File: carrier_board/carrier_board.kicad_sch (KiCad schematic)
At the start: 4 parts, among them J1 47571-0001, U1 Pico

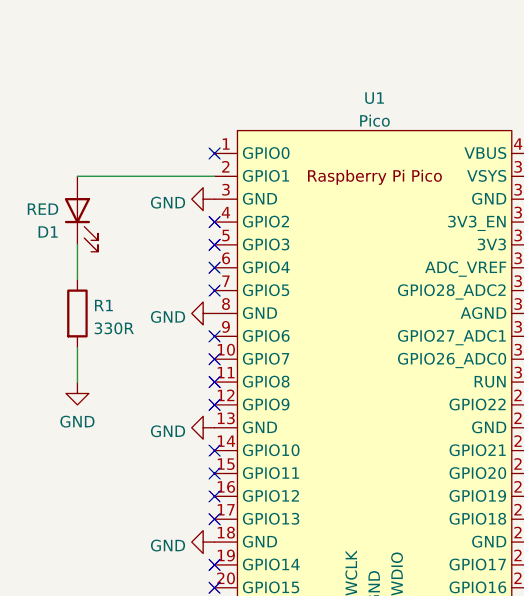
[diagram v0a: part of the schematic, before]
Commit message: Change red LED from GP2 to GP4 to free up UART RX
Also add label to LED on board
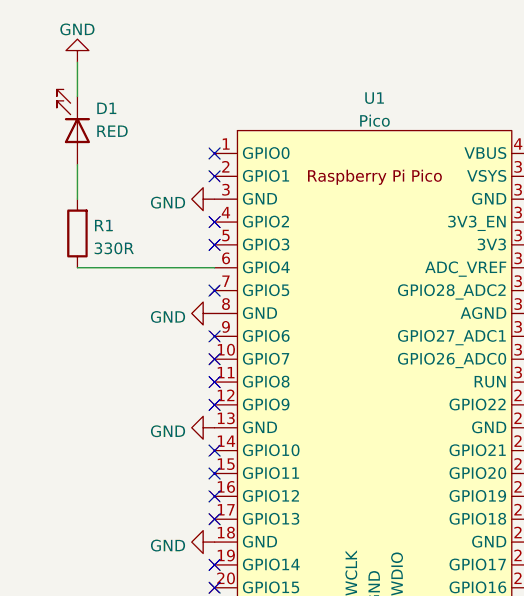
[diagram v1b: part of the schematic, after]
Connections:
- net GND: now also D1.1 (K); no longer R1.2
- net at R1.1: now also U1.6 (GPIO4); no longer D1.1 (K)
- net at D1.2 (A): now also R1.2; no longer U1.2 (GPIO1)
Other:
- moved on the sheet: D1, R1
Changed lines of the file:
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@@
     (title "OpenReset Carrier Board")
     (date "2022-03-20")
-    (rev "v1")
+    (rev "v1a")
     (company "cyanic")
   )
@@
   (no_connect (at 127 68.58))
   (no_connect (at 127 63.5))
-  (no_connect (at 127 60.96))
   (no_connect (at 127 58.42))
   (no_connect (at 127 55.88))
@@
   (no_connect (at 127 81.28))
   (no_connect (at 127 76.2))
+  (no_connect (at 127 50.8))
   (no_connect (at 127 96.52))
   (no_connect (at 142.24 101.6))
@@
     (stroke (width 0) (type default) (color 0 0 0 0))
   )
-  (wire (pts (xy 111.76 69.85) (xy 111.76 73.66))
-    (stroke (width 0) (type default) (color 0 0 0 0))
-  )
   (wire (pts (xy 124.46 129.54) (xy 124.46 134.62))
     (stroke (width 0) (type default) (color 0 0 0 0))
@@
     (stroke (width 0) (type default) (color 0 0 0 0))
   )
-  (wire (pts (xy 111.76 50.8) (xy 127 50.8))
+  (wire (pts (xy 111.76 38.1) (xy 111.76 41.91))
     (stroke (width 0) (type default) (color 0 0 0 0))
   )
@@
     (stroke (width 0) (type default) (color 0 0 0 0))
   )
-  (wire (pts (xy 111.76 58.42) (xy 111.76 62.23))
+  (wire (pts (xy 111.76 60.96) (xy 127 60.96))
+    (stroke (width 0) (type default) (color 0 0 0 0))
+  )
+  (wire (pts (xy 111.76 49.53) (xy 111.76 53.34))
     (stroke (width 0) (type default) (color 0 0 0 0))
   )
@@
     (pin "1")
   )
-  (symbol (lib_id "Device:LED") (at 111.76 54.61 90) (unit 1)
+  (symbol (lib_id "Device:LED") (at 111.76 45.72 270) (unit 1)
     (in_bom yes) (on_board yes)
-    (property "Reference" "D1" (id 0) (at 109.728 57.0322 90)
+    (property "Reference" "D1" (id 0) (at 113.792 43.2978 90)
       (effects (font (size 1.27 1.27)) (justify left))
     )
-    (property "Value" "RED" (id 1) (at 109.728 54.4953 90)
+    (property "Value" "RED" (id 1) (at 113.792 45.8347 90)
       (effects (font (size 1.27 1.27)) (justify left))
     )
-    (property "Footprint" "Library:LED_0603_1608Metric_Pad1.05x0.95mm_HandSolder" (id 2) (at 111.76 54.61 0)
-      (effects (font (size 1.27 1.27)) hide)
-    )
-    (property "Datasheet" "~" (id 3) (at 111.76 54.61 0)
+    (property "Footprint" "Library:LED_0603_1608Metric_Pad1.05x0.95mm_HandSolder" (id 2) (at 111.76 45.72 0)
+      (effects (font (size 1.27 1.27)) hide)
+    )
+    (property "Datasheet" "~" (id 3) (at 111.76 45.72 0)
       (effects (font (size 1.27 1.27)) hide)
     )
@@
     (pin "1")
   )
-  (symbol (lib_id "Device:R") (at 111.76 66.04 0) (unit 1)
-    (in_bom yes) (on_board yes) (fields_autoplaced)
-    (property "Reference" "R1" (id 0) (at 113.538 65.2053 0)
-      (effects (font (size 1.27 1.27)) (justify left))
-    )
-    (property "Value" "330R" (id 1) (at 113.538 67.7422 0)
-      (effects (font (size 1.27 1.27)) (justify left))
-    )
-    (property "Footprint" "Library:R_0603_1608Metric_Pad0.98x0.95mm_HandSolder" (id 2) (at 109.982 66.04 90)
-      (effects (font (size 1.27 1.27)) hide)
-    )
-    (property "Datasheet" "~" (id 3) (at 111.76 66.04 0)
+  (symbol (lib_id "Device:R") (at 111.76 57.15 180) (unit 1)
+    (in_bom yes) (on_board yes) (fields_autoplaced)
+    (property "Reference" "R1" (id 0) (at 113.538 56.3153 0)
+      (effects (font (size 1.27 1.27)) (justify right))
+    )
+    (property "Value" "330R" (id 1) (at 113.538 58.8522 0)
+      (effects (font (size 1.27 1.27)) (justify right))
+    )
+    (property "Footprint" "Library:R_0603_1608Metric_Pad0.98x0.95mm_HandSolder" (id 2) (at 113.538 57.15 90)
+      (effects (font (size 1.27 1.27)) hide)
+    )
+    (property "Datasheet" "~" (id 3) (at 111.76 57.15 0)
       (effects (font (size 1.27 1.27)) hide)
     )
@@
     )
     (property "Datasheet" "" (id 3) (at 162.56 58.42 0)
+      (effects (font (size 1.27 1.27)) hide)
+    )
+    (pin "1")
+  )
+  (symbol (lib_id "power:GND") (at 111.76 38.1 180) (unit 1)
+    (in_bom yes) (on_board yes) (fields_autoplaced)
+    (property "Reference" "#PWR0114" (id 0) (at 111.76 31.75 0)
+      (effects (font (size 1.27 1.27)) hide)
+    )
+    (property "Value" "GND" (id 1) (at 111.76 34.5242 0))
+    (property "Footprint" "" (id 2) (at 111.76 38.1 0)
+      (effects (font (size 1.27 1.27)) hide)
+    )
+    (property "Datasheet" "" (id 3) (at 111.76 38.1 0)
       (effects (font (size 1.27 1.27)) hide)
     )
@@
     (pin "P8")
   )
-  (symbol (lib_id "power:GND") (at 111.76 73.66 0) (unit 1)
-    (in_bom yes) (on_board yes) (fields_autoplaced)
-    (property "Reference" "#PWR0114" (id 0) (at 111.76 80.01 0)
-      (effects (font (size 1.27 1.27)) hide)
-    )
-    (property "Value" "GND" (id 1) (at 111.76 78.1034 0))
-    (property "Footprint" "" (id 2) (at 111.76 73.66 0)
-      (effects (font (size 1.27 1.27)) hide)
-    )
-    (property "Datasheet" "" (id 3) (at 111.76 73.66 0)
-      (effects (font (size 1.27 1.27)) hide)
-    )
-    (pin "1")
-  )
   (sheet_instances
     (path "/" (page "1"))
@@
       (reference "#PWR0113") (unit 1) (value "GND") (footprint "")
     )
-    (path "/fb09765e-b715-419e-ad46-726f9bf7e352"
+    (path "/dd479a80-227b-44d6-b0fa-58cd4309c382"
       (reference "#PWR0114") (unit 1) (value "GND") (footprint "")
     )
